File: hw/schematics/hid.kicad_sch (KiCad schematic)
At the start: 108 parts, among them M1 SK8701-01-004-MODULE, M2 SK8701-01-004-SENSOR, SW1 SW_Push, SW10 SW_Push, SW11 SW_Push, SW12 SW_Push, SW13 SW_Push, SW14 SW_Push, SW15 SW_Push, SW16 SW_Push, SW17 SW_Push, SW18 SW_Push, SW19 SW_Push, SW2 SW_Push, SW20 SW_Push, SW21 SW_Push, SW22 SW_Push, SW23 SW_Push, SW3 SW_Push, SW4 SW_Push, SW5 SW_Push, SW6 SW_Push, SW7 SW_Push, SW8 SW_Push, SW9 SW_Push, U4 SN74LVC138ARGY

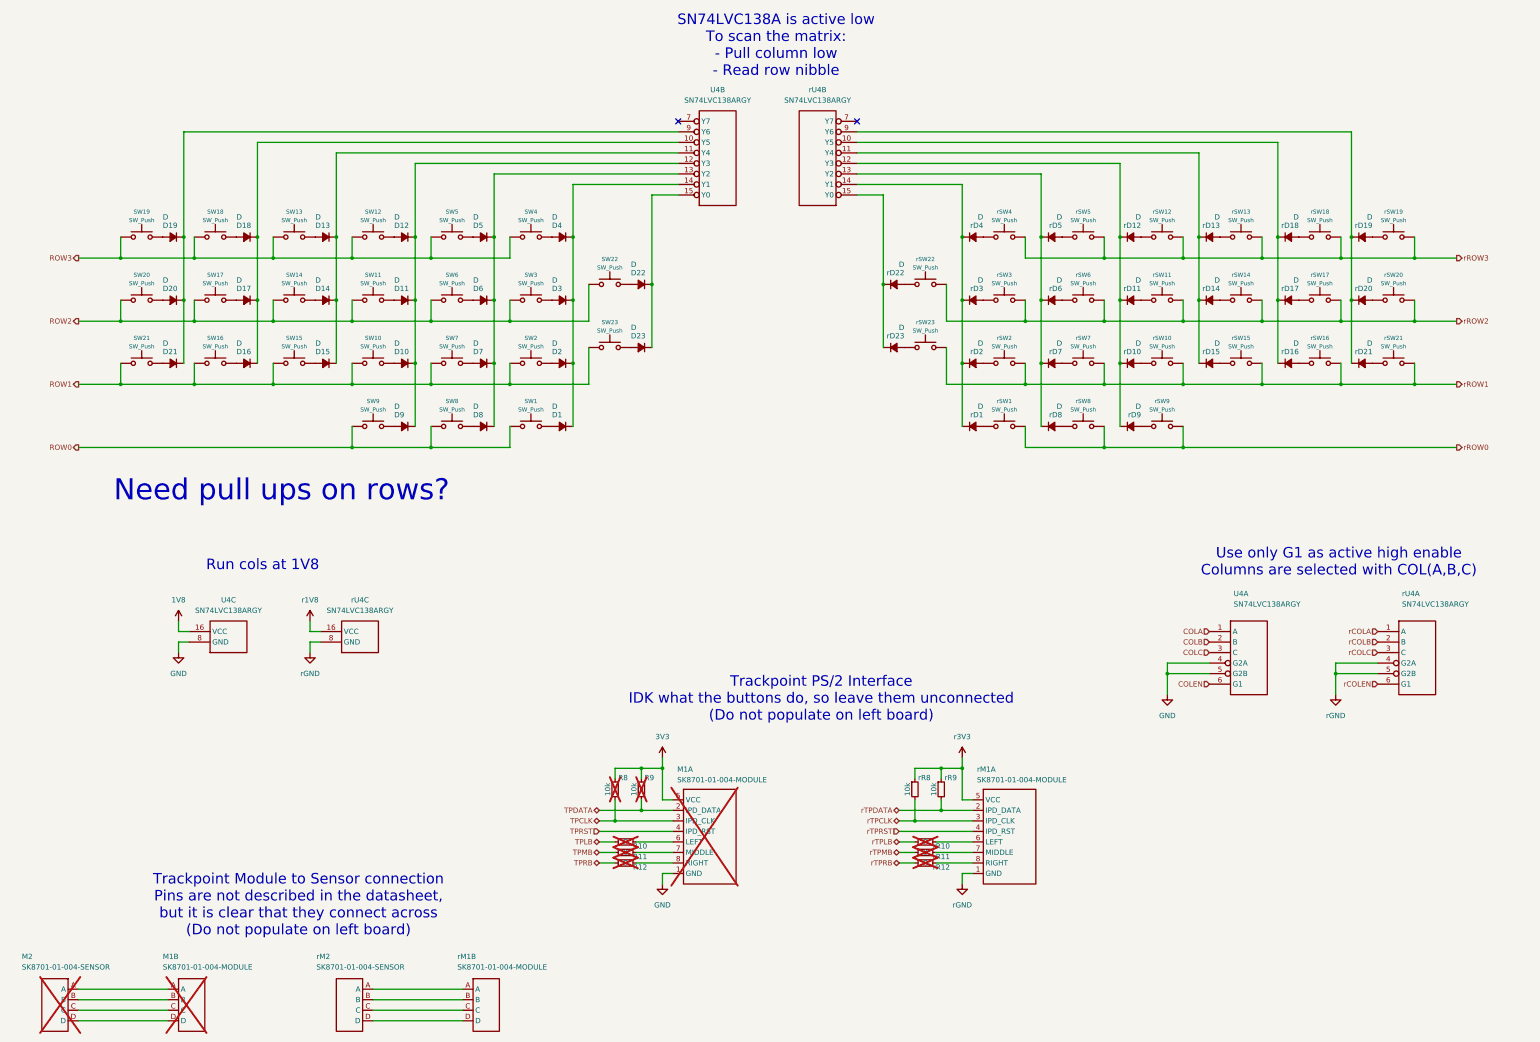
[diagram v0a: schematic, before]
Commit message: Remove SN74LVC138A as we now have enough pins on the UP
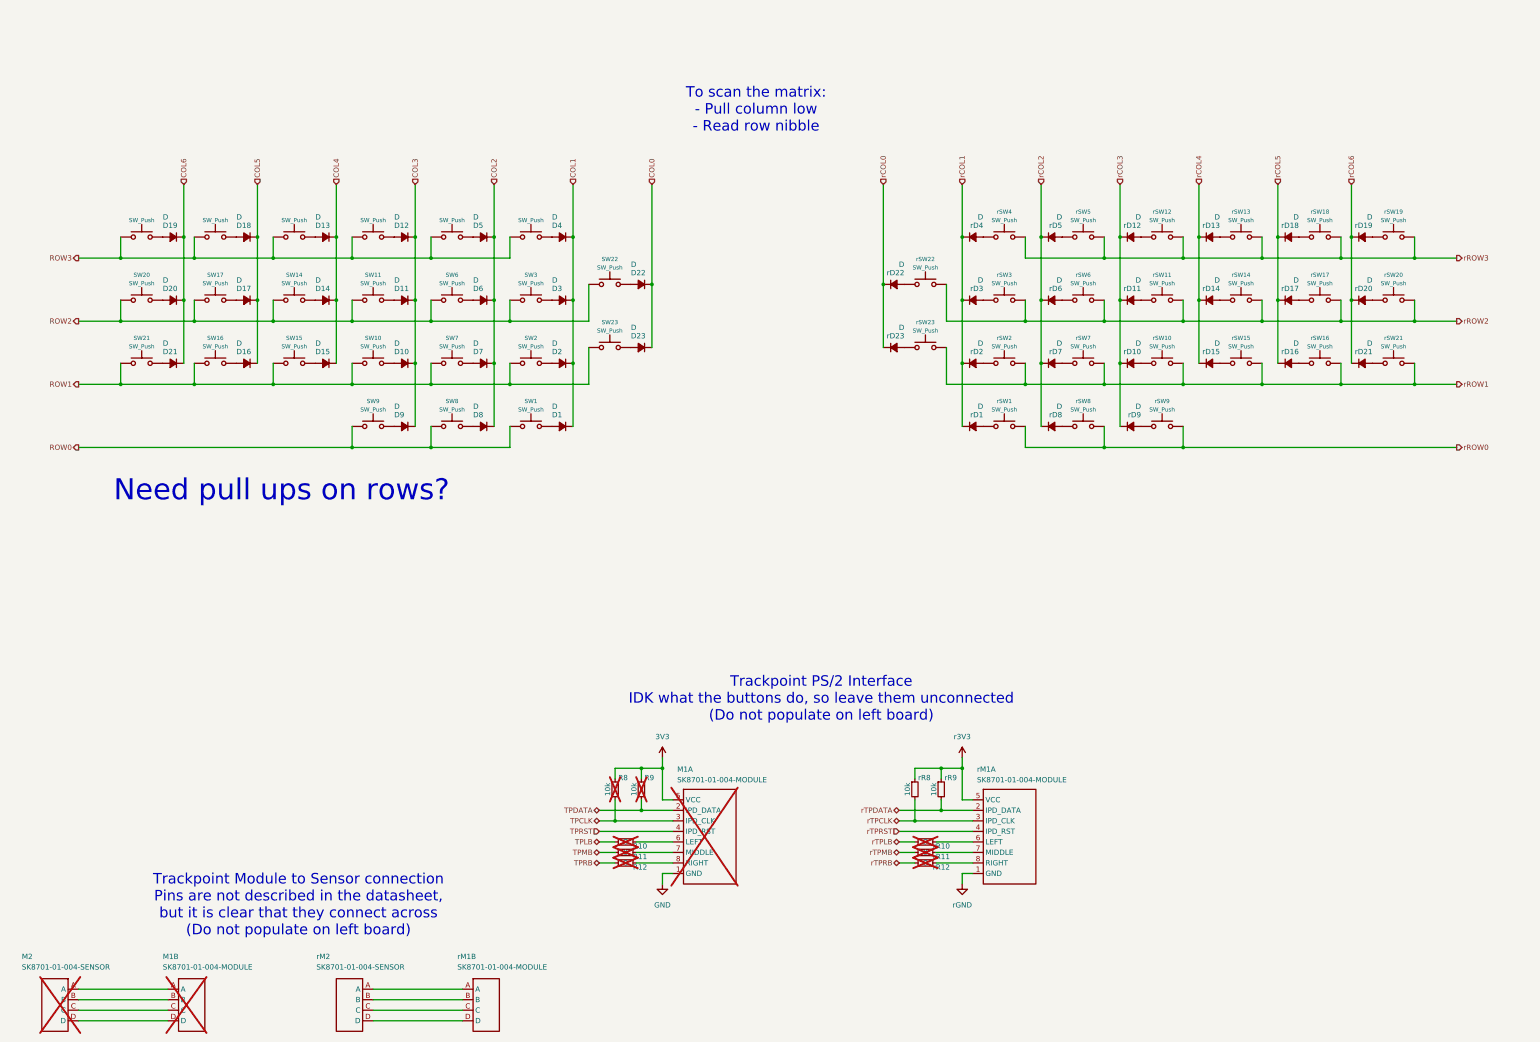
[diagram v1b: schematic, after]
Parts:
- removed U4, rU4: SN74LVC138ARGY, symbol Alidade:SN74LVC138ARGY
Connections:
- net rCOL1: now reaches rD1.1 (K), rD2.1 (K), rD3.1 (K), rD4.1 (K)
- net COL2: now reaches D5.1 (K), D6.1 (K), D7.1 (K), D8.1 (K)
- net COL5: now reaches D16.1 (K), D17.1 (K), D18.1 (K)
- net COL4: now reaches D13.1 (K), D14.1 (K), D15.1 (K)
- net COL3: now reaches D10.1 (K), D11.1 (K), D12.1 (K), D9.1 (K)
- net COL1: now reaches D1.1 (K), D2.1 (K), D3.1 (K), D4.1 (K)
- net COL0: now reaches D22.1 (K), D23.1 (K)
- net COL6: now reaches D19.1 (K), D20.1 (K), D21.1 (K)
- net rCOL5: now reaches rD16.1 (K), rD17.1 (K), rD18.1 (K)
- net rCOL6: now reaches rD19.1 (K), rD20.1 (K), rD21.1 (K)
- net rCOL2: now reaches rD5.1 (K), rD6.1 (K), rD7.1 (K), rD8.1 (K)
- net rCOL4: now reaches rD13.1 (K), rD14.1 (K), rD15.1 (K)
- net rCOL3: now reaches rD10.1 (K), rD11.1 (K), rD12.1 (K), rD9.1 (K)
- net rCOL0: now reaches rD22.1 (K), rD23.1 (K)
- no-connect marks 2 -> 0
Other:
- note added: "To scan the matrix: - Pull column low - Read row nibble"
- note removed: "Run cols at 1V8"
- note removed: "SN74LVC138A is active low To scan the matrix: - Pull column low - Read row nibble"
- note removed: "Use only G1 as active high enable Columns are selected with COL(A,B,C)"

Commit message: SK8701-01-005 sensor footprint with diamond plate
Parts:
- M2, rM2: footprint (none) -> Alidade:SK8707-01-SENSOR
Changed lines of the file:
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@@
 			)
 		)
-		(property "Footprint" ""
+		(property "Footprint" "Alidade:SK8707-01-SENSOR"
 			(at 115.57 250.19 0)
 			(effects
@@
 			)
 		)
-		(property "Footprint" ""
+		(property "Footprint" "Alidade:SK8707-01-SENSOR"
 			(at 44.45 250.19 0)
 			(effects

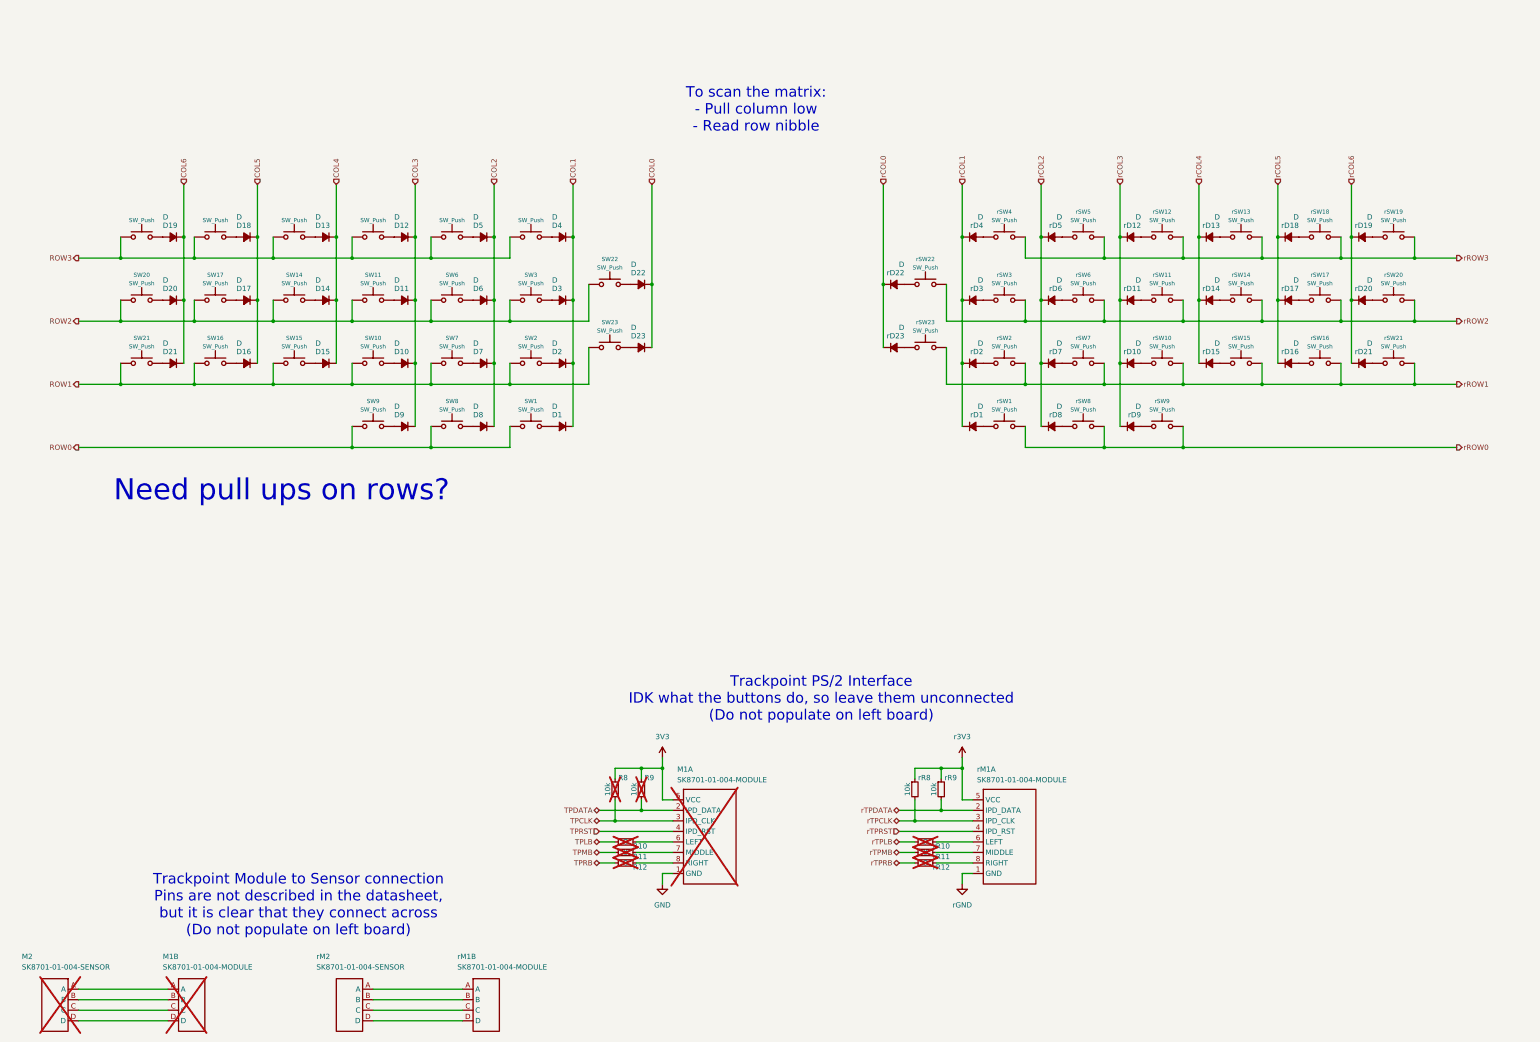
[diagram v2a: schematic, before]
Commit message: pull ups on rows
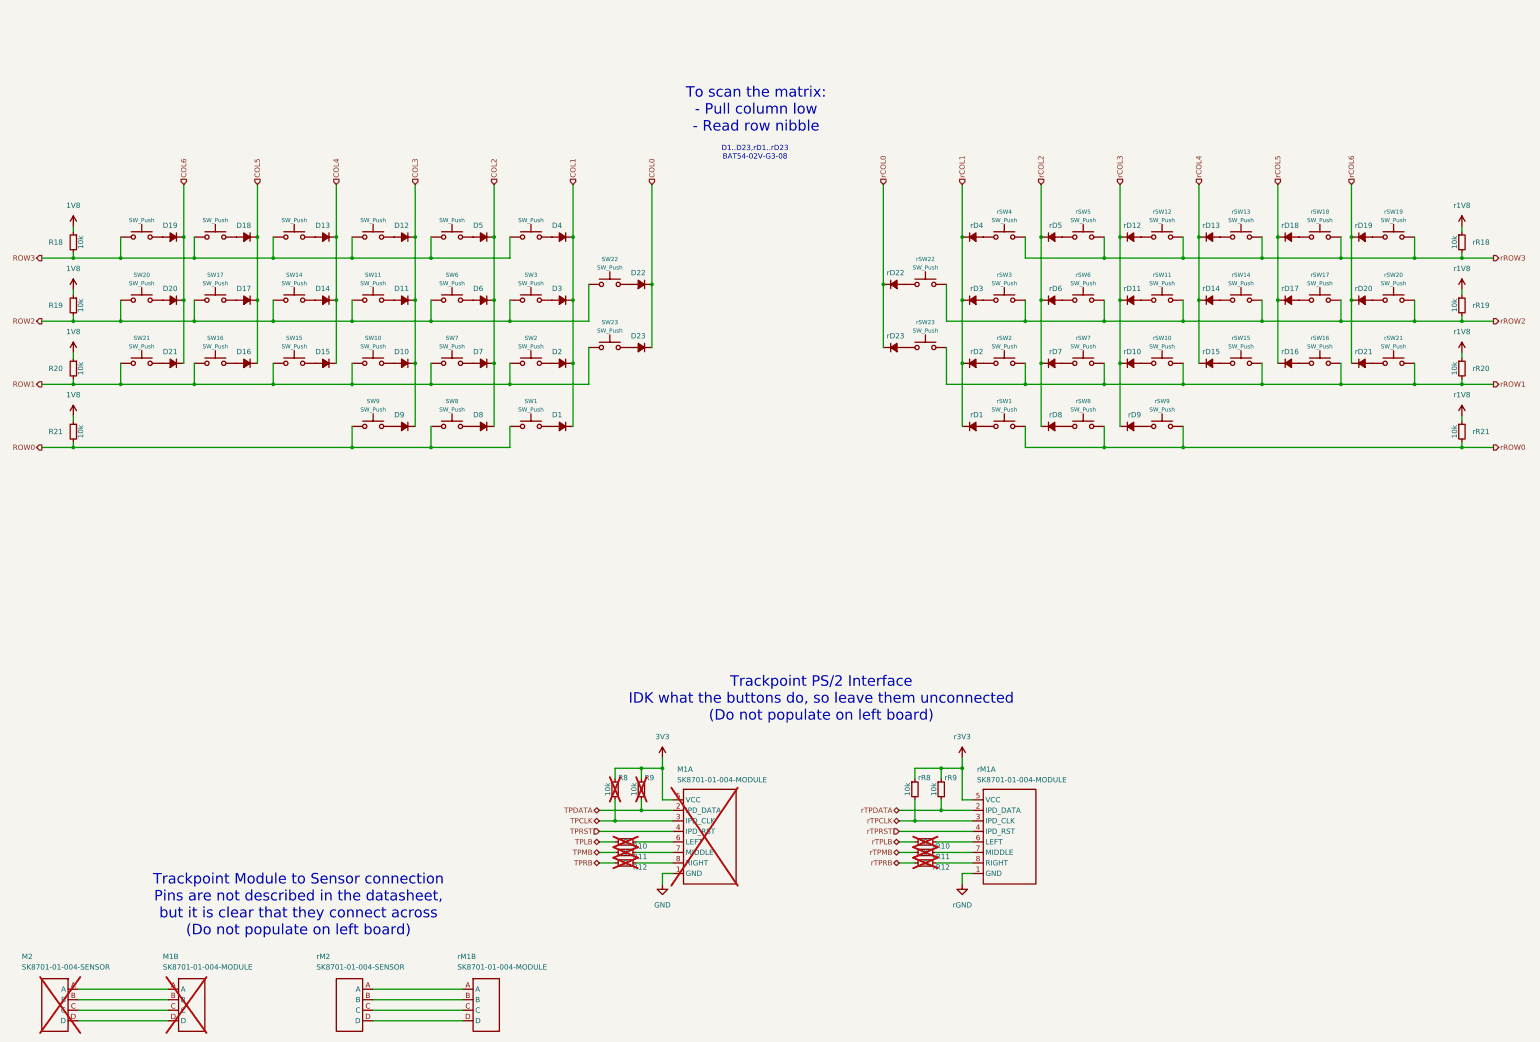
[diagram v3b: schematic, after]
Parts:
- added R18, R19, R20, R21, rR18, rR19, rR20, rR21: 10k, symbol Alidade:R
- D1, D10, D11, D12, D13, D14, D15, D16, D17, D18, D19, D2, D20, D21, D22, D23, D3, D4, D5, D6, D7, D8, D9, rD1, rD10, rD11, rD12, rD13, rD14, rD15, rD16, rD17, rD18, rD19, rD2, rD20, rD21, rD22, rD23, rD3, rD4, rD5, rD6, rD7, rD8, rD9: value D -> BAT54-02V-G3-08
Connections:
- net ROW0: now also R21.2
- net ROW1: now also R20.2
- net ROW2: now also R19.2
- net ROW3: now also R18.2
- net rROW0: now also rR21.2
- net rROW1: now also rR20.2
- net rROW2: now also rR19.2
- net rROW3: now also rR18.2
- new net 1V8: R18.1, R19.1, R20.1, R21.1
- new net r1V8: rR18.1, rR19.1, rR20.1, rR21.1
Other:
- note added: "D1..D23,rD1..rD23 BAT54-02V-G3-08"
- note removed: "Need pull ups on rows?"

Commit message: 0603 footprint
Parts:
- D1, D10, D11, D12, D13, D14, D15, D16, D17, D18, D19, D2, D20, D21, D22, D23, D3, D4, D5, D6, D7, D8, D9, rD1, rD10, rD11, rD12, rD13, rD14, rD15, rD16, rD17, rD18, rD19, rD2, rD20, rD21, rD22, rD23, rD3, rD4, rD5, rD6, rD7, rD8, rD9: footprint (none) -> Alidade:SOD-523
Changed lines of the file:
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@@
 			)
 		)
-		(property "Footprint" ""
+		(property "Footprint" "Alidade:SOD-523"
 			(at 260.35 71.12 90)
 			(effects
@@
 			)
 		)
-		(property "Footprint" ""
+		(property "Footprint" "Alidade:SOD-523"
 			(at 142.24 101.6 90)
 			(effects
@@
 			)
 		)
-		(property "Footprint" ""
+		(property "Footprint" "Alidade:SOD-523"
 			(at 85.09 71.12 90)
 			(effects
@@
 			)
 		)
-		(property "Footprint" ""
+		(property "Footprint" "Alidade:SOD-523"
 			(at 104.14 71.12 90)
 			(effects
@@
 			)
 		)
-		(property "Footprint" ""
+		(property "Footprint" "Alidade:SOD-523"
 			(at 336.55 101.6 90)
 			(effects
@@
 			)
 		)
-		(property "Footprint" ""
+		(property "Footprint" "Alidade:SOD-523"
 			(at 354.33 86.36 90)
 			(effects
@@
 			)
 		)
-		(property "Footprint" ""
+		(property "Footprint" "Alidade:SOD-523"
 			(at 279.4 116.84 90)
 			(effects
@@
 			)
 		)
-		(property "Footprint" ""
+		(property "Footprint" "Alidade:SOD-523"
 			(at 317.5 86.36 90)
 			(effects
@@
 			)
 		)
-		(property "Footprint" ""
+		(property "Footprint" "Alidade:SOD-523"
 			(at 317.5 71.12 90)
 			(effects
@@
 			)
 		)
-		(property "Footprint" ""
+		(property "Footprint" "Alidade:SOD-523"
 			(at 298.45 101.6 90)
 			(effects
@@
 			)
 		)
-		(property "Footprint" ""
+		(property "Footprint" "Alidade:SOD-523"
 			(at 161.29 116.84 90)
 			(effects
@@
 			)
 		)
-		(property "Footprint" ""
+		(property "Footprint" "Alidade:SOD-523"
 			(at 161.29 86.36 90)
 			(effects
@@
 			)
 		)
-		(property "Footprint" ""
+		(property "Footprint" "Alidade:SOD-523"
 			(at 354.33 101.6 90)
 			(effects
@@
 			)
 		)
-		(property "Footprint" ""
+		(property "Footprint" "Alidade:SOD-523"
 			(at 180.34 82.55 90)
 			(effects
@@
 			)
 		)
-		(property "Footprint" ""
+		(property "Footprint" "Alidade:SOD-523"
 			(at 260.35 116.84 90)
 			(effects
@@
 			)
 		)
-		(property "Footprint" ""
+		(property "Footprint" "Alidade:SOD-523"
 			(at 123.19 71.12 90)
 			(effects
@@
 			)
 		)
-		(property "Footprint" ""
+		(property "Footprint" "Alidade:SOD-523"
 			(at 67.31 101.6 90)
 			(effects
@@
 			)
 		)
-		(property "Footprint" ""
+		(property "Footprint" "Alidade:SOD-523"
 			(at 85.09 101.6 90)
 			(effects
@@
 			)
 		)
-		(property "Footprint" ""
+		(property "Footprint" "Alidade:SOD-523"
 			(at 104.14 86.36 90)
 			(effects
@@
 			)
 		)
-		(property "Footprint" ""
+		(property "Footprint" "Alidade:SOD-523"
 			(at 123.19 101.6 90)
 			(effects
@@
 			)
 		)
-		(property "Footprint" ""
+		(property "Footprint" "Alidade:SOD-523"
 			(at 279.4 86.36 90)
 			(effects
@@
 			)
 		)
-		(property "Footprint" ""
+		(property "Footprint" "Alidade:SOD-523"
 			(at 336.55 71.12 90)
 			(effects
@@
 			)
 		)
-		(property "Footprint" ""
+		(property "Footprint" "Alidade:SOD-523"
 			(at 260.35 101.6 90)
 			(effects
@@
 			)
 		)
-		(property "Footprint" ""
+		(property "Footprint" "Alidade:SOD-523"
 			(at 67.31 71.12 90)
 			(effects
@@
 			)
 		)
-		(property "Footprint" ""
+		(property "Footprint" "Alidade:SOD-523"
 			(at 142.24 71.12 90)
 			(effects
@@
 			)
 		)
-		(property "Footprint" ""
+		(property "Footprint" "Alidade:SOD-523"
 			(at 67.31 86.36 90)
 			(effects
@@
 			)
 		)
-		(property "Footprint" ""
+		(property "Footprint" "Alidade:SOD-523"
 			(at 241.3 82.55 90)
 			(effects
@@
 			)
 		)
-		(property "Footprint" ""
+		(property "Footprint" "Alidade:SOD-523"
 			(at 161.29 101.6 90)
 			(effects
@@
 			)
 		)
-		(property "Footprint" ""
+		(property "Footprint" "Alidade:SOD-523"
 			(at 336.55 86.36 90)
 			(effects
@@
 			)
 		)
-		(property "Footprint" ""
+		(property "Footprint" "Alidade:SOD-523"
 			(at 142.24 116.84 90)
 			(effects
@@
 			)
 		)
-		(property "Footprint" ""
+		(property "Footprint" "Alidade:SOD-523"
 			(at 241.3 97.79 90)
 			(effects
@@
 			)
 		)
-		(property "Footprint" ""
+		(property "Footprint" "Alidade:SOD-523"
 			(at 161.29 71.12 90)
 			(effects
@@
 			)
 		)
-		(property "Footprint" ""
+		(property "Footprint" "Alidade:SOD-523"
 			(at 279.4 71.12 90)
 			(effects
@@
 			)
 		)
-		(property "Footprint" ""
+		(property "Footprint" "Alidade:SOD-523"
 			(at 298.45 86.36 90)
 			(effects
@@
 			)
 		)
-		(property "Footprint" ""
+		(property "Footprint" "Alidade:SOD-523"
 			(at 123.19 116.84 90)
 			(effects
@@
 			)
 		)
-		(property "Footprint" ""
+		(property "Footprint" "Alidade:SOD-523"
 			(at 85.09 86.36 90)
 			(effects
@@
 			)
 		)
-		(property "Footprint" ""
+		(property "Footprint" "Alidade:SOD-523"
 			(at 279.4 101.6 90)
 			(effects
@@
 			)
 		)
-		(property "Footprint" ""
+		(property "Footprint" "Alidade:SOD-523"
 			(at 354.33 71.12 90)
 			(effects
@@
 			)
 		)
-		(property "Footprint" ""
+		(property "Footprint" "Alidade:SOD-523"
 			(at 104.14 101.6 90)
 			(effects
@@
 			)
 		)
-		(property "Footprint" ""
+		(property "Footprint" "Alidade:SOD-523"
 			(at 142.24 86.36 90)
 			(effects
@@
 			)
 		)
-		(property "Footprint" ""
+		(property "Footprint" "Alidade:SOD-523"
 			(at 260.35 86.36 90)
 			(effects
@@
 			)
 		)
-		(property "Footprint" ""
+		(property "Footprint" "Alidade:SOD-523"
 			(at 317.5 101.6 90)
 			(effects
@@
 			)
 		)
-		(property "Footprint" ""
+		(property "Footprint" "Alidade:SOD-523"
 			(at 180.34 97.79 90)
 			(effects
@@
 			)
 		)
-		(property "Footprint" ""
+		(property "Footprint" "Alidade:SOD-523"
 			(at 298.45 116.84 90)
 			(effects
@@
 			)
 		)
-		(property "Footprint" ""
+		(property "Footprint" "Alidade:SOD-523"
 			(at 298.45 71.12 90)
 			(effects
@@
 			)
 		)
-		(property "Footprint" ""
+		(property "Footprint" "Alidade:SOD-523"
 			(at 123.19 86.36 90)
 			(effects
